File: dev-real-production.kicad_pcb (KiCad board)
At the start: 4 copper layers, 105 x 105 mm, 320 parts, among them IC1 ICM-42670-P, IC2 ENS161-BLGT_LGA9_T&R_1k5, J1 VIN_IN, J10 USB-C USB2 DEBUG, J11 ARM_JTAG_10, J12 SOP0_SELECT, J13 SOP1_SELECT, J14 Conn_01x03, J15 Conn_01x03, J16 ARM_JTAG_10, J17 USB-C Receptacle USB2, J18 Conn_01x03_Pin, J19 Cortex SWD/JTAG, J2 TP_EN_PG, J20 USB-C USB2 DEVICE, J21 HR911105A MAGJACK, J22 Conn_02x10_Counter_Clockwise, J23 Conn_02x04_Odd_Even, J3 TP_SW_FB, J4 USB-C Receptacle USB2, J5 Conn_01x03_Pin, J6 ARM_Cortex_Debug_10, J7 SMA_ANT_50OHM, J8 3V3_IN, U1 MMC5633NJL, U10 USBLC6-2P6, U11 FT230XS-R, U12 FT230XS-R, U13 IWRL6432BDBAAMFR, U14 MX25R1635FZUIH0, U15 MX25R1635FZUIH0, U16 AMS1117-1.8, U17 THS8136, U18 MM8108-MF15457, U19 AP2112K-1.8, U2 LPS22HH, U20 PGA113AIDGSR, U21 AD9609BCPZRL7-80, U22 MCP6D11T-E/MS, U23 STM32H7S3Z8T6, U24 LAN8742A-CZ-TR, U25 USBLC6-2SC6, U3 MIC28516T-E/PHA, U4 RP2350B, U5 XCC1352R1F3RGZR, U6 XMSSJJ3G0PA-054, U7 TLV75518PDBV, U8 TLV75518PDBVR, U9 USBLC6-2P6, Y1 12MHz ABM8-272-T3, Y2 48MHz, Y3 40MHz, Y4 40MHz, Y5 24MHz, Y6 32.768kHz, Y7 25MHz

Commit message: fix: ETH TX differential pair skew matched to 0.000mm
Added a 5.274mm length-matching extension to /STM32H7/PHY_TXN on Top Layer so both legs of the Ethernet TX pair are now exactly equal length. DRC verified: 0 errors, 0 unconnected items.

Regenerated all production Gerbers, drill files, positions and reports from the updated PCB.
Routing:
- net /STM32H7/PHY_TXN: track 45.9 -> 51.2 mm
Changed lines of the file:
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@@
 	)
 	(gr_line
-		(start 4 4)
-		(end 40 4)
+		(start 70 4)
+		(end 70 44)
 		(stroke
 			(width 0.1)
@@
 	)
 	(gr_line
-		(start 4 34)
-		(end 4 4)
+		(start 40 82)
+		(end 40 104)
 		(stroke
 			(width 0.1)
@@
 	)
 	(gr_line
-		(start 4 82)
-		(end 40 82)
+		(start 40 104)
+		(end 4 104)
 		(stroke
 			(width 0.1)
@@
 	)
 	(gr_line
-		(start 4 86)
-		(end 4 36)
+		(start 76 78)
+		(end 76 104)
 		(stroke
 			(width 0.1)
@@
 	)
 	(gr_line
-		(start 4 104)
-		(end 4 82)
+		(start 4 34)
+		(end 4 4)
 		(stroke
 			(width 0.1)
@@
 	)
 	(gr_line
-		(start 40 4)
-		(end 70 4)
+		(start 104 55)
+		(end 104 104)
 		(stroke
 			(width 0.1)
@@
 	)
 	(gr_line
-		(start 40 34)
-		(end 4 34)
+		(start 4 104)
+		(end 4 82)
 		(stroke
 			(width 0.1)
@@
 	)
 	(gr_line
-		(start 40 44)
-		(end 40 4)
+		(start 78 55)
+		(end 104 55)
 		(stroke
 			(width 0.1)
@@
 	)
 	(gr_line
-		(start 40 82)
-		(end 40 104)
+		(start 78 78)
+		(end 55 78)
 		(stroke
 			(width 0.1)
@@
 	)
 	(gr_line
-		(start 40 104)
-		(end 4 104)
+		(start 78 104)
+		(end 78 55)
 		(stroke
 			(width 0.1)
@@
 	)
 	(gr_line
-		(start 44 78)
-		(end 76 78)
+		(start 104 54)
+		(end 70 54)
 		(stroke
 			(width 0.1)
@@
 	)
 	(gr_line
-		(start 44 104)
-		(end 44 78)
+		(start 44 78)
+		(end 76 78)
 		(stroke
 			(width 0.1)
@@
 	)
 	(gr_line
-		(start 55 36)
-		(end 55 86)
+		(start 104 4)
+		(end 104 54)
 		(stroke
 			(width 0.1)
@@
 	)
 	(gr_line
-		(start 55 52)
-		(end 78 52)
+		(start 70 4)
+		(end 104 4)
 		(stroke
 			(width 0.1)
@@
 	)
 	(gr_line
-		(start 55 78)
-		(end 55 52)
+		(start 40 4)
+		(end 70 4)
 		(stroke
 			(width 0.1)
@@
 	)
 	(gr_line
-		(start 55 86)
-		(end 4 86)
+		(start 40 44)
+		(end 40 4)
 		(stroke
 			(width 0.1)
@@
 	)
 	(gr_line
-		(start 70 4)
-		(end 70 44)
+		(start 4 4)
+		(end 40 4)
 		(stroke
 			(width 0.1)
@@
 	)
 	(gr_line
-		(start 70 4)
-		(end 104 4)
+		(start 4 86)
+		(end 4 36)
 		(stroke
 			(width 0.1)
@@
 	)
 	(gr_line
-		(start 70 44)
-		(end 40 44)
+		(start 55 86)
+		(end 4 86)
 		(stroke
 			(width 0.1)
@@
 	)
 	(gr_line
-		(start 70 54)
-		(end 70 4)
+		(start 44 104)
+		(end 44 78)
 		(stroke
 			(width 0.1)
@@
 	)
 	(gr_line
-		(start 76 78)
-		(end 76 104)
+		(start 76 104)
+		(end 44 104)
 		(stroke
 			(width 0.1)
@@
 	)
 	(gr_line
-		(start 76 104)
-		(end 44 104)
+		(start 55 52)
+		(end 78 52)
 		(stroke
 			(width 0.1)
@@
 	)
 	(gr_line
-		(start 78 52)
-		(end 78 78)
+		(start 4 82)
+		(end 40 82)
 		(stroke
 			(width 0.1)
@@
 	)
 	(gr_line
-		(start 78 55)
-		(end 104 55)
+		(start 78 52)
+		(end 78 78)
 		(stroke
 			(width 0.1)
@@
 	)
 	(gr_line
-		(start 78 78)
-		(end 55 78)
+		(start 70 54)
+		(end 70 4)
 		(stroke
 			(width 0.1)
@@
 	)
 	(gr_line
-		(start 78 104)
-		(end 78 55)
+		(start 55 36)
+		(end 55 86)
 		(stroke
 			(width 0.1)
@@
 	)
 	(gr_line
-		(start 104 4)
-		(end 104 54)
+		(start 40 34)
+		(end 4 34)
 		(stroke
 			(width 0.1)
@@
 	)
 	(gr_line
-		(start 104 54)
-		(end 70 54)
+		(start 104 104)
+		(end 78 104)
 		(stroke
 			(width 0.1)
@@
 	)
 	(gr_line
-		(start 104 55)
-		(end 104 104)
+		(start 55 78)
+		(end 55 52)
 		(stroke
 			(width 0.1)
@@
 	)
 	(gr_line
-		(start 104 104)
-		(end 78 104)
+		(start 70 44)
+		(end 40 44)
 		(stroke
 			(width 0.1)
@@
 	)
 	(gr_line
-		(start 0 0)
-		(end 105 0)
+		(start 105 0)
+		(end 105 105)
 		(stroke
 			(width 0.05)
@@
 	)
 	(gr_line
-		(start 105 0)
-		(end 105 105)
+		(start 105 105)
+		(end 0 105)
 		(stroke
 			(width 0.05)
@@
 	)
 	(gr_line
-		(start 105 105)
-		(end 0 105)
+		(start 0 0)
+		(end 105 0)
 		(stroke
 			(width 0.05)
@@
 		(layer "Edge.Cuts")
 	)
-	(gr_text "XCC1352 RF"
-		(at 5 6 0)
+	(gr_text "RP2350"
+		(at 45 80 0)
 		(layer "Dwgs.User")
 		(effects
@@
 		)
 	)
-	(gr_text "STM32H7"
-		(at 5 38 0)
+	(gr_text "IWRL6432 Radar"
+		(at 41 6 0)
 		(layer "Dwgs.User")
 		(effects
@@
 		)
 	)
-	(gr_text "MM8108"
-		(at 5 84 0)
+	(gr_text "Root IO"
+		(at 79 57 0)
 		(layer "Dwgs.User")
 		(effects
@@
 		)
 	)
-	(gr_text "IWRL6432 Radar"
-		(at 41 6 0)
+	(gr_text "XCC1352 RF"
+		(at 5 6 0)
 		(layer "Dwgs.User")
 		(effects
@@
 		)
 	)
-	(gr_text "RP2350"
-		(at 45 80 0)
+	(gr_text "STM32H7"
+		(at 5 38 0)
 		(layer "Dwgs.User")
 		(effects
@@
 		)
 	)
-	(gr_text "Root IO"
-		(at 79 57 0)
+	(gr_text "MM8108"
+		(at 5 84 0)
 		(layer "Dwgs.User")
 		(effects
@@
 		(layer "F.Cu")
 		(net 307)
+	)
+	(segment
+		(start 17.947597 76.878638)
+		(end 12.673597 76.878638)
+		(width 0.15)
+		(layer "F.Cu")
+		(net 307)

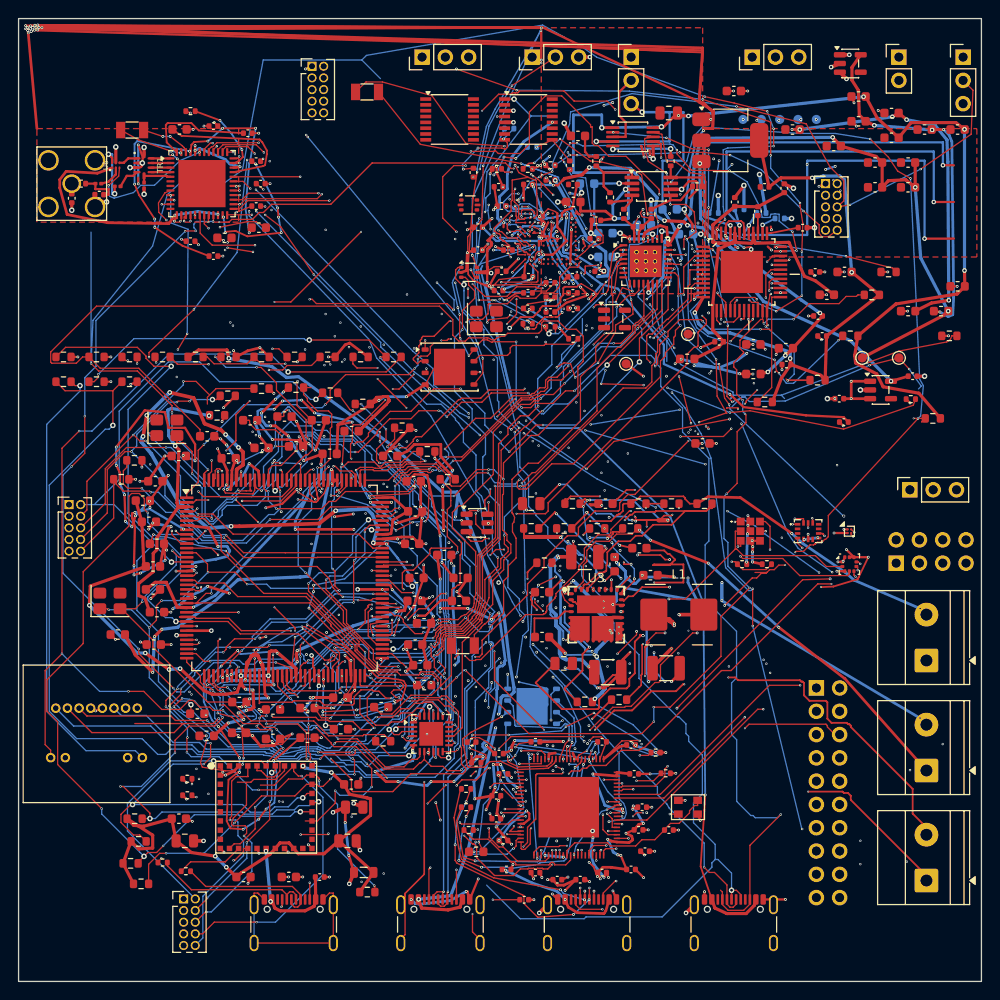
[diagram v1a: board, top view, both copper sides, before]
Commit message: route: save manual connector pair tuning candidate
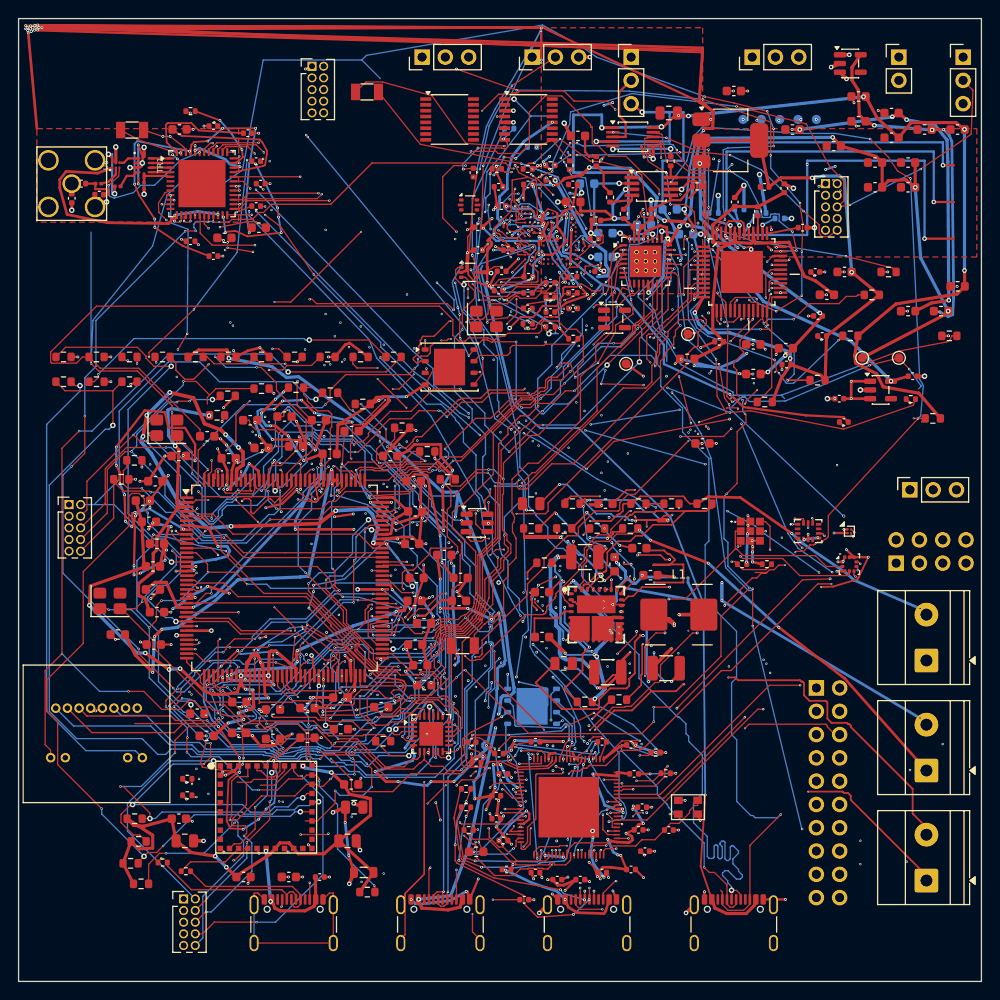
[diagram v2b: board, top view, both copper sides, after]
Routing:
- net /IWRL6432BD/USB_DP_CONN: track 114.6 -> 100.6 mm
- net /IWRL6432BD/FT_TXD: track 43.7 -> 38.1 mm
- net /STM32H7/USB_FS_DM: track 28.1 -> 32.6 mm
- net /AD9609/CLK_N: track 76.4 -> 74.0 mm
